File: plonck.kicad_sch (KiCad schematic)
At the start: 132 parts, among them J1 USB_C_Receptacle_USB2.0, J2 Battery_connector, J3 Conn_01x06, Q1 Q_PMOS_GSD, SW1 SW_Push, U1 SRV05-4, U2 TP4054-42-SOT25-R, U3 nRF52840_holyiot_18010, U4 XC6206PxxxMR-Regulator_Linear

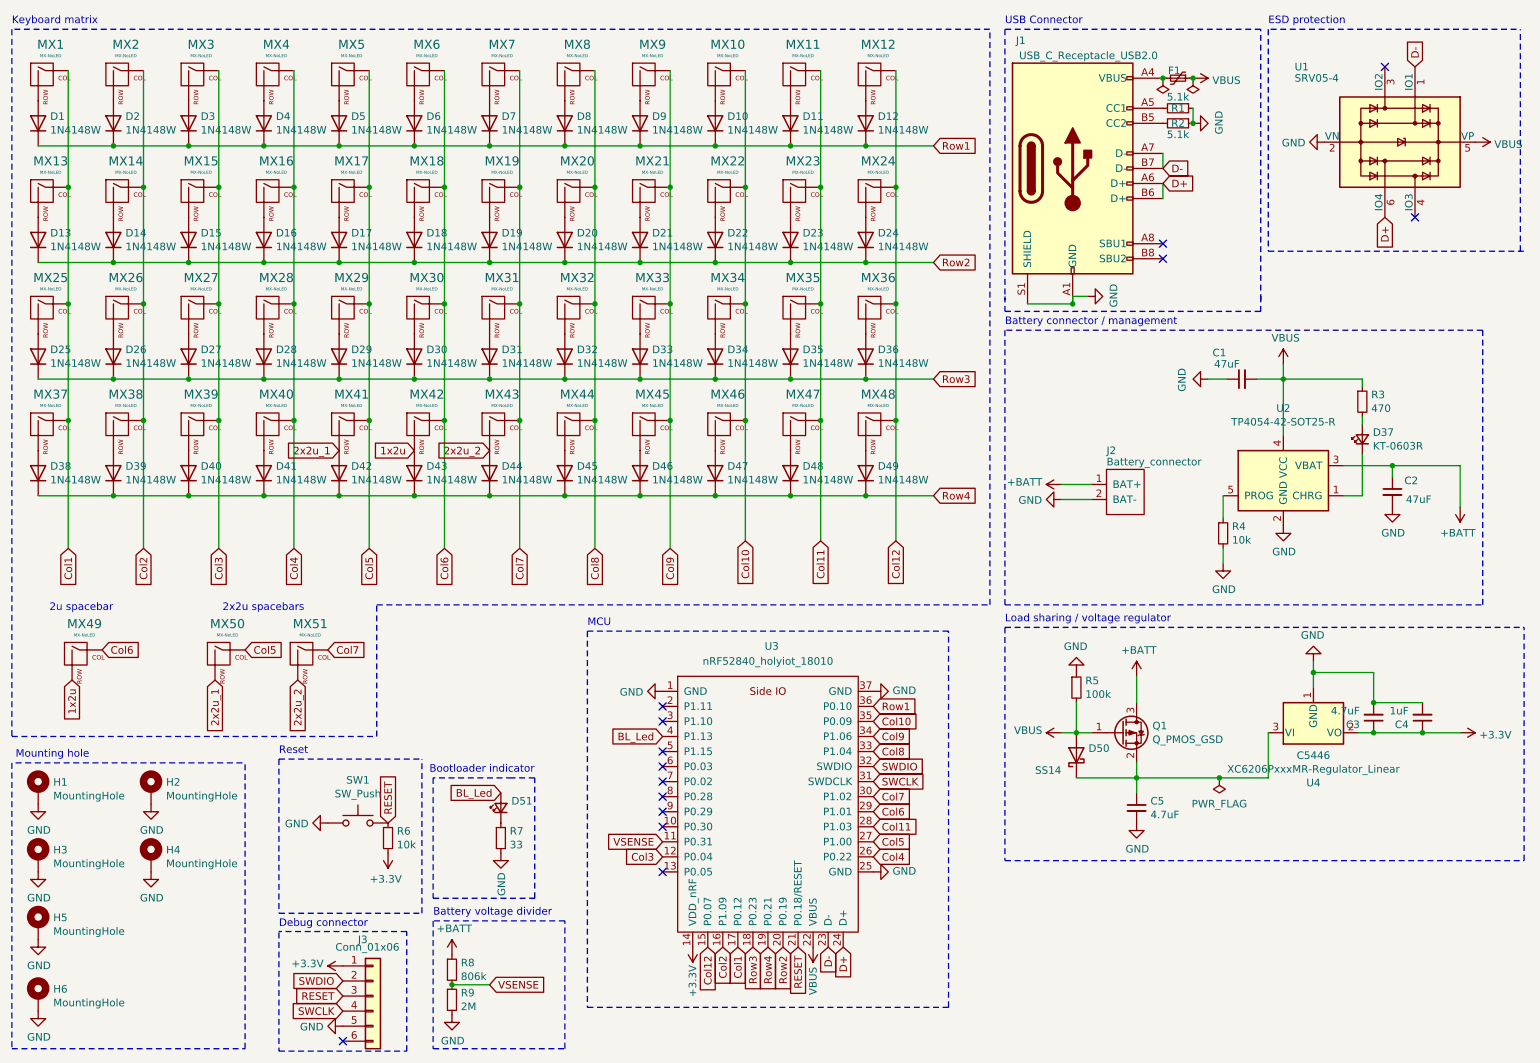
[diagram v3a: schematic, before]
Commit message: various updates
* switched to smd usb-c port
* updated various lcsc part numbers
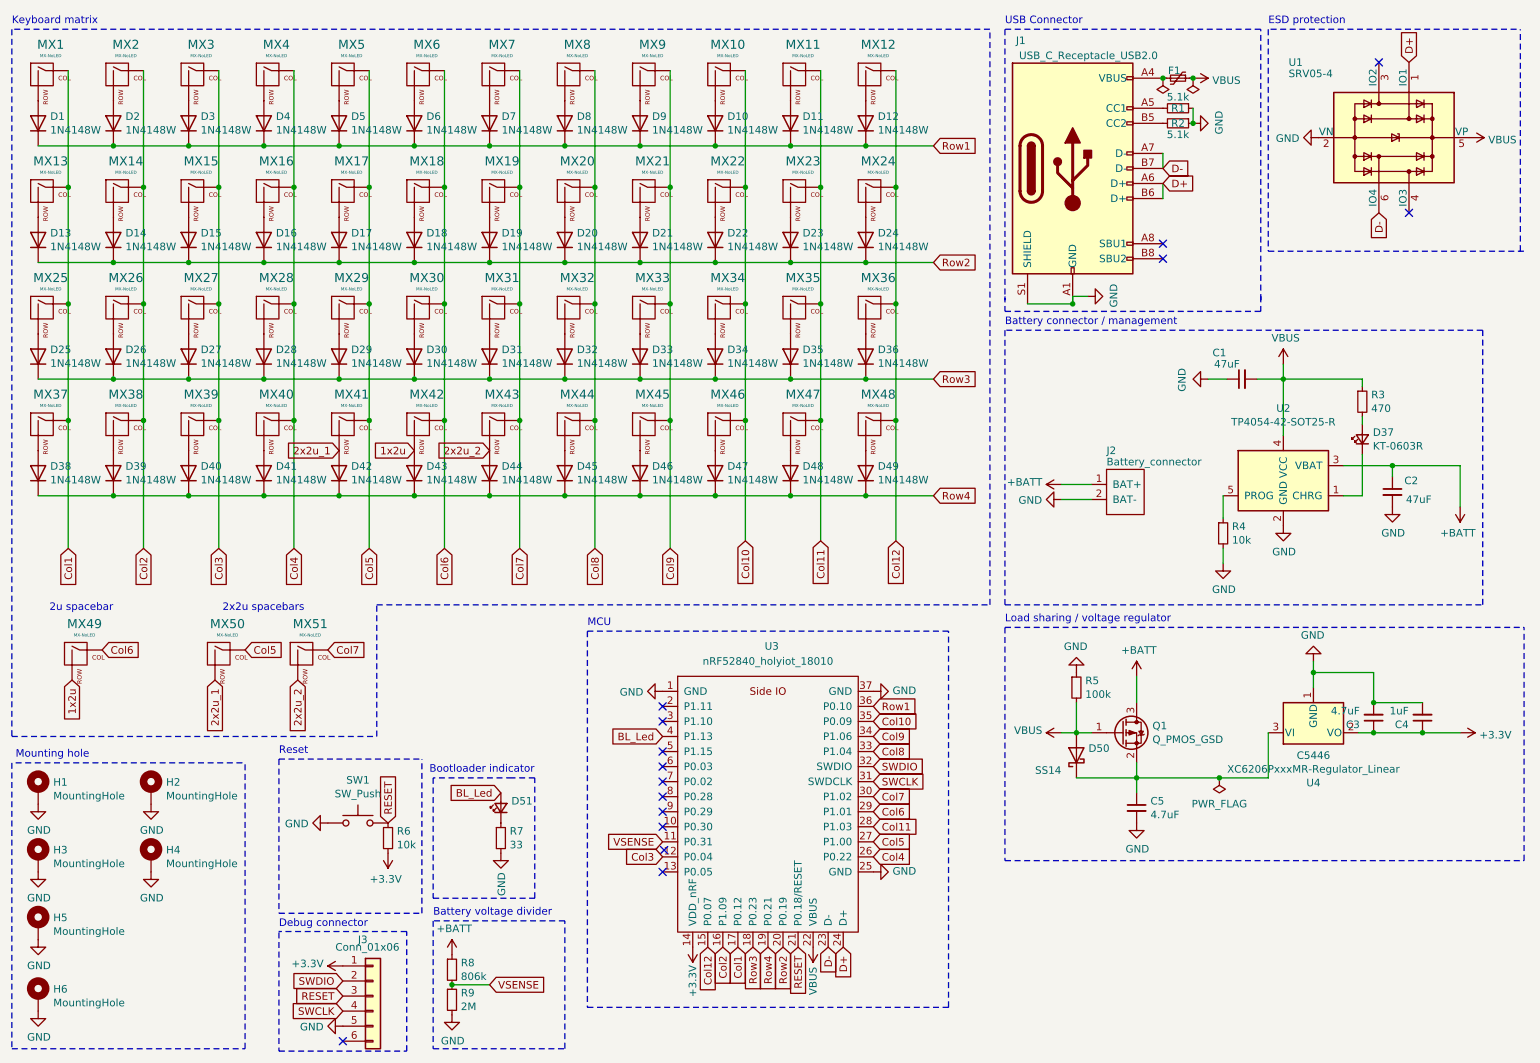
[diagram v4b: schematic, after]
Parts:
- C3, C5: LCSC C162266 -> C19666
- C4: LCSC C525329 -> C15849
- F1: LCSC (none) -> C182974
- J1: footprint Connector_USB:USB_C_Receptacle_GCT_USB4085 -> Connector_USB:USB_C_Receptacle_HRO_TYPE-C-31-M-12; LCSC (none) -> C165948
- R4: Digikey RMCF0603JG10K0TR-ND -> (none)
- R6: LCSC (none) -> C25804
- R8: LCSC (none) -> C23250
- R9: LCSC (none) -> C22976
- SW1: LCSC (none) -> C115357
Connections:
- net D+: now also U1.1 (IO1); no longer U1.6 (IO4)
- net D-: now also U1.6 (IO4); no longer U1.1 (IO1)
- no-connect marks 14 -> 15
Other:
- moved on the sheet: U1
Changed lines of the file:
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@@
   (no_connect (at 125.095 151.765))
   (no_connect (at 125.095 159.385))
+  (no_connect (at 125.349 155.702))
   (no_connect (at 209.55 53.34))
   (no_connect (at 209.55 55.88))
-  (no_connect (at 247.015 23.495))
-  (no_connect (at 252.095 48.895))
+  (no_connect (at 245.999 22.733))
+  (no_connect (at 251.079 48.133))
   (wire (pts (xy 19.685 36.83) (xy 32.385 36.83))
     (stroke (width 0) (type solid) (color 0 0 0 0))
@@
     )
   )
-  (global_label "D+" (shape input) (at 247.015 48.895 270) (fields_autoplaced)
+  (global_label "D-" (shape input) (at 245.999 48.133 270) (fields_autoplaced)
     (effects (font (size 1.27 1.27)) (justify right))
-    (property "Intersheet References" "${INTERSHEET_REFS}" (id 0) (at 0 0 0)
-      (effects (font (size 1.27 1.27)) hide)
+    (property "Intersheet References" "${INTERSHEET_REFS}" (id 0) (at 245.9196 53.3885 90)
+      (effects (font (size 1.27 1.27)) (justify right) hide)
     )
   )
-  (global_label "D-" (shape input) (at 252.095 23.495 90) (fields_autoplaced)
+  (global_label "D+" (shape input) (at 251.079 22.733 90) (fields_autoplaced)
     (effects (font (size 1.27 1.27)) (justify left))
-    (property "Intersheet References" "${INTERSHEET_REFS}" (id 0) (at 0 0 0)
-      (effects (font (size 1.27 1.27)) hide)
+    (property "Intersheet References" "${INTERSHEET_REFS}" (id 0) (at 250.9996 17.4775 90)
+      (effects (font (size 1.27 1.27)) (justify left) hide)
     )
   )
@@
     (pin "1")
   )
-  (symbol (lib_id "power:VBUS") (at 262.255 36.195 270) (unit 1)
+  (symbol (lib_id "power:VBUS") (at 261.239 35.433 270) (unit 1)
     (in_bom yes) (on_board yes)
-    (property "Reference" "#PWR04" (id 0) (at 258.445 36.195 0)
+    (property "Reference" "#PWR04" (id 0) (at 257.429 35.433 0)
       (effects (font (size 1.27 1.27)) hide)
     )
-    (property "Value" "VBUS" (id 1) (at 265.4808 36.576 90)
+    (property "Value" "VBUS" (id 1) (at 264.4648 35.814 90)
       (effects (font (size 1.27 1.27)) (justify left))
     )
-    (property "Footprint" "" (id 2) (at 262.255 36.195 0)
+    (property "Footprint" "" (id 2) (at 261.239 35.433 0)
       (effects (font (size 1.27 1.27)) hide)
     )
-    (property "Datasheet" "" (id 3) (at 262.255 36.195 0)
+    (property "Datasheet" "" (id 3) (at 261.239 35.433 0)
       (effects (font (size 1.27 1.27)) hide)
     )
@@
     (pin "1")
   )
-  (symbol (lib_id "power:GND") (at 236.855 36.195 270) (unit 1)
+  (symbol (lib_id "power:GND") (at 235.839 35.433 270) (unit 1)
     (in_bom yes) (on_board yes)
-    (property "Reference" "#PWR03" (id 0) (at 230.505 36.195 0)
+    (property "Reference" "#PWR03" (id 0) (at 229.489 35.433 0)
       (effects (font (size 1.27 1.27)) hide)
     )
-    (property "Value" "GND" (id 1) (at 233.6038 36.322 90)
+    (property "Value" "GND" (id 1) (at 232.5878 35.56 90)
       (effects (font (size 1.27 1.27)) (justify right))
     )
-    (property "Footprint" "" (id 2) (at 236.855 36.195 0)
+    (property "Footprint" "" (id 2) (at 235.839 35.433 0)
       (effects (font (size 1.27 1.27)) hide)
     )
-    (property "Datasheet" "" (id 3) (at 236.855 36.195 0)
+    (property "Datasheet" "" (id 3) (at 235.839 35.433 0)
       (effects (font (size 1.27 1.27)) hide)
     )
@@
       (effects (font (size 1.27 1.27)) hide)
     )
+    (property "LCSC" "C25804" (id 4) (at 78.74 153.67 0)
+      (effects (font (size 1.27 1.27)) hide)
+    )
     (pin "1")
     (pin "2")
@@
       (effects (font (size 1.27 1.27)) hide)
     )
-    (property "LCSC" "" (id 4) (at 89.535 175.895 0)
+    (property "LCSC" "C23250" (id 4) (at 89.535 175.895 0)
       (effects (font (size 1.27 1.27)) hide)
     )
@@
       (effects (font (size 1.27 1.27)) hide)
     )
-    (property "LCSC" "" (id 4) (at 89.535 180.975 0)
+    (property "LCSC" "C22976" (id 4) (at 89.535 180.975 0)
       (effects (font (size 1.27 1.27)) hide)
     )
@@
       (effects (font (size 1.27 1.27)) hide)
     )
-    (property "Digikey" "RMCF0603JG10K0TR-ND" (id 4) (at 219.71 102.235 0)
+    (property "Digikey" "" (id 4) (at 219.71 102.235 0)
       (effects (font (size 1.27 1.27)) hide)
     )
@@
       (effects (font (size 1.27 1.27)) hide)
     )
-    (property "LCSC" "" (id 4) (at 212.09 25.4 0)
+    (property "LCSC" "C182974" (id 4) (at 212.09 25.4 0)
       (effects (font (size 1.27 1.27)) hide)
     )
@@
       (effects (font (size 1.27 1.27)) hide)
     )
-    (property "Datasheet" "~" (id 3) (at 205.105 148.59 0)
+    (property "Datasheet" "https://datasheet.lcsc.com/lcsc/1810261514_Samsung-Electro-Mechanics-CL10A475KO8NNNC_C19666.pdf" (id 3) (at 205.105 148.59 0)
       (effects (font (size 1.27 1.27)) hide)
     )
-    (property "LCSC" "C162266" (id 4) (at 205.105 148.59 0)
+    (property "LCSC" "C19666" (id 4) (at 205.105 148.59 0)
       (effects (font (size 1.27 1.27)) hide)
     )
@@
       (effects (font (size 1.27 1.27)) hide)
     )
-    (property "Datasheet" "~" (id 3) (at 245.11 133.35 0)
+    (property "Datasheet" "https://datasheet.lcsc.com/lcsc/1810261514_Samsung-Electro-Mechanics-CL10A475KO8NNNC_C19666.pdf" (id 3) (at 245.11 133.35 0)
       (effects (font (size 1.27 1.27)) hide)
     )
-    (property "LCSC" "C162266" (id 4) (at 245.11 133.35 0)
+    (property "LCSC" "C19666" (id 4) (at 245.11 133.35 0)
       (effects (font (size 1.27 1.27)) hide)
     )
@@
       (effects (font (size 1.27 1.27)) hide)
     )
-    (property "Datasheet" "~" (id 3) (at 253.365 133.35 0)
+    (property "Datasheet" "https://datasheet.lcsc.com/lcsc/1810261812_Samsung-Electro-Mechanics-CL10A105KB8NNNC_C15849.pdf" (id 3) (at 253.365 133.35 0)
       (effects (font (size 1.27 1.27)) hide)
     )
-    (property "LCSC" "C525329" (id 4) (at 253.365 133.35 0)
+    (property "LCSC" "C15849" (id 4) (at 253.365 133.35 0)
       (effects (font (size 1.27 1.27)) hide)
     )
@@
       (effects (font (size 1.27 1.27)) hide)
     )
+    (property "LCSC" "C115357" (id 4) (at 73.66 151.13 0)
+      (effects (font (size 1.27 1.27)) hide)
+    )
     (pin "1")
     (pin "2")
@@
     (pin "5")
   )
-  (symbol (lib_id "Power_Protection:SRV05-4") (at 249.555 36.195 270) (unit 1)
+  (symbol (lib_id "Power_Protection:SRV05-4") (at 248.539 35.433 270) (unit 1)
     (in_bom yes) (on_board yes)
-    (property "Reference" "U1" (id 0) (at 231.775 23.495 90)
+    (property "Reference" "U1" (id 0) (at 230.759 22.733 90)
       (effects (font (size 1.27 1.27)) (justify left))
     )
-    (property "Value" "SRV05-4" (id 1) (at 231.775 25.4 90)
+    (property "Value" "SRV05-4" (id 1) (at 230.759 24.638 90)
       (effects (font (size 1.27 1.27)) (justify left))
     )
-    (property "Footprint" "Package_TO_SOT_SMD:SOT-23-6" (id 2) (at 238.125 53.975 0)
+    (property "Footprint" "Package_TO_SOT_SMD:SOT-23-6" (id 2) (at 237.109 53.213 0)
       (effects (font (size 1.27 1.27)) hide)
     )
-    (property "Datasheet" "http://www.onsemi.com/pub/Collateral/SRV05-4-D.PDF" (id 3) (at 249.555 36.195 0)
+    (property "Datasheet" "http://www.onsemi.com/pub/Collateral/SRV05-4-D.PDF" (id 3) (at 248.539 35.433 0)
       (effects (font (size 1.27 1.27)) hide)
     )
-    (property "LCSC" "C782797" (id 4) (at 249.555 36.195 90)
+    (property "LCSC" "C782797" (id 4) (at 248.539 35.433 90)
       (effects (font (size 1.27 1.27)) hide)
     )
@@
     (property "Reference" "J1" (id 0) (at 185.547 19.05 0))
     (property "Value" "USB_C_Receptacle_USB2.0" (id 1) (at 196.977 21.59 0))
-    (property "Footprint" "Connector_USB:USB_C_Receptacle_GCT_USB4085" (id 2) (at 198.12 40.64 0)
+    (property "Footprint" "Connector_USB:USB_C_Receptacle_HRO_TYPE-C-31-M-12" (id 2) (at 198.12 40.64 0)
+      (effects (font (size 1.27 1.27)) hide)
+    )
+    (property "Datasheet" "https://datasheet.lcsc.com/szlcsc/1811131825_Korean-Hroparts-Elec-TYPE-C-31-M-12_C165948.pdf" (id 3) (at 198.12 40.64 0)
       (effects (font (size 1.27 1.27)) hide)
     )
-    (property "Datasheet" "https://www.usb.org/sites/default/files/documents/usb_type-c.zip" (id 3) (at 198.12 40.64 0)
+    (property "LCSC" "C165948" (id 4) (at 194.31 40.64 0)
       (effects (font (size 1.27 1.27)) hide)
     )
@@
     )
     (path "/c6b48aca-e6ec-415b-bd56-226c73d7f498"
-      (reference "J1") (unit 1) (value "USB_C_Receptacle_USB2.0") (footprint "Connector_USB:USB_C_Receptacle_GCT_USB4085")
+      (reference "J1") (unit 1) (value "USB_C_Receptacle_USB2.0") (footprint "Connector_USB:USB_C_Receptacle_HRO_TYPE-C-31-M-12")
     )
     (path "/00000000-0000-0000-0000-0000605544b8"

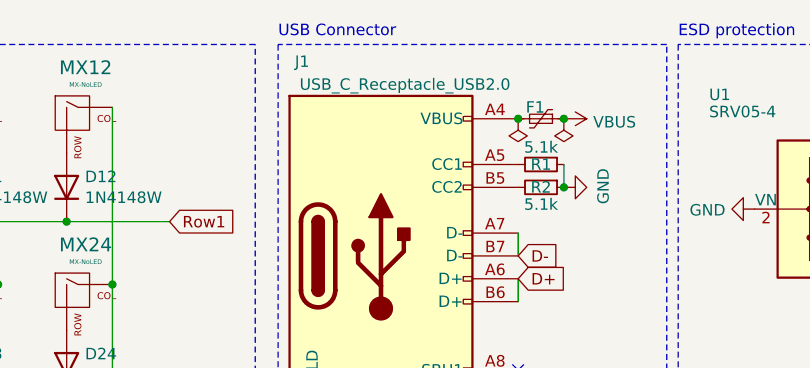
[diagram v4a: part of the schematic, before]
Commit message: adding/fixing lcsc part numbers
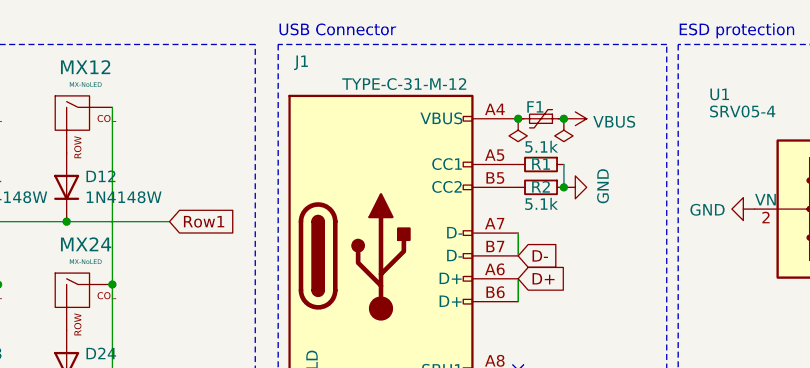
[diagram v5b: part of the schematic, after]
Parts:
- J1: value USB_C_Receptacle_USB2.0 -> TYPE-C-31-M-12
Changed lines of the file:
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@@
     (in_bom yes) (on_board yes)
     (property "Reference" "J1" (id 0) (at 185.547 19.05 0))
-    (property "Value" "USB_C_Receptacle_USB2.0" (id 1) (at 196.977 21.59 0))
+    (property "Value" "TYPE-C-31-M-12" (id 1) (at 196.977 21.59 0))
     (property "Footprint" "Connector_USB:USB_C_Receptacle_HRO_TYPE-C-31-M-12" (id 2) (at 198.12 40.64 0)
       (effects (font (size 1.27 1.27)) hide)
@@
     )
     (path "/c6b48aca-e6ec-415b-bd56-226c73d7f498"
-      (reference "J1") (unit 1) (value "USB_C_Receptacle_USB2.0") (footprint "Connector_USB:USB_C_Receptacle_HRO_TYPE-C-31-M-12")
+      (reference "J1") (unit 1) (value "TYPE-C-31-M-12") (footprint "Connector_USB:USB_C_Receptacle_HRO_TYPE-C-31-M-12")
     )
     (path "/00000000-0000-0000-0000-0000605544b8"

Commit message: housekeeping
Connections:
- no-connect marks 15 -> 14
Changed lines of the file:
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@@
   (junction (at 164.465 63.5) (diameter 0.9144) (color 0 0 0 0))
   (junction (at 164.465 83.185) (diameter 0.9144) (color 0 0 0 0))
+  (junction (at 190.373 63.5) (diameter 0.9144) (color 0 0 0 0))
   (junction (at 194.31 63.5) (diameter 0.9144) (color 0 0 0 0))
   (junction (at 194.945 135.89) (diameter 0.9144) (color 0 0 0 0))
@@
   (no_connect (at 125.095 151.765))
   (no_connect (at 125.095 159.385))
-  (no_connect (at 125.349 155.702))
   (no_connect (at 209.55 53.34))
   (no_connect (at 209.55 55.88))
@@
     (stroke (width 0) (type solid) (color 0 0 0 0))
   )
-  (wire (pts (xy 186.69 63.5) (xy 194.31 63.5))
+  (wire (pts (xy 186.69 63.5) (xy 190.373 63.5))
+    (stroke (width 0) (type solid) (color 0 0 0 0))
+  )
+  (wire (pts (xy 190.373 63.5) (xy 194.31 63.5))
     (stroke (width 0) (type solid) (color 0 0 0 0))
   )
@@
     (pin "1")
   )
+  (symbol (lib_id "power:PWR_FLAG") (at 190.373 63.5 0) (unit 1)
+    (in_bom yes) (on_board yes)
+    (property "Reference" "#FLG?" (id 0) (at 190.373 61.595 0)
+      (effects (font (size 1.27 1.27)) hide)
+    )
+    (property "Value" "PWR_FLAG" (id 1) (at 190.373 59.1058 0)
+      (effects (font (size 1.27 1.27)) hide)
+    )
+    (property "Footprint" "" (id 2) (at 190.373 63.5 0)
+      (effects (font (size 1.27 1.27)) hide)
+    )
+    (property "Datasheet" "~" (id 3) (at 190.373 63.5 0)
+      (effects (font (size 1.27 1.27)) hide)
+    )
+    (pin "1")
+  )
   (symbol (lib_id "power:PWR_FLAG") (at 209.55 25.4 180) (unit 1)
     (in_bom yes) (on_board yes)
@@
       (reference "#FLG03") (unit 1) (value "PWR_FLAG") (footprint "")
     )
+    (path "/70e030db-bf10-4ba5-90f9-dd1165563a4d"
+      (reference "#FLG?") (unit 1) (value "PWR_FLAG") (footprint "")
+    )
     (path "/00000000-0000-0000-0000-0000607c6c1d"
